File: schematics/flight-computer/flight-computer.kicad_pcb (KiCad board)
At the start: 4 copper layers, 80 x 80 mm, 116 parts, among them J1 BATT, J2 CHG, J3 SWD, J4 BLACKBOX, J5 USB C, J6 GPS, J7 TELEM, J8 BMI-S-201, J9 Expansion Slot, Q1 Si9933CDY, Q2 BSS138, U1 MAX14787E, U10 LTC4002-ES8, U11 MAX604, U12 MAX604, U2 STM32F405RGT6, U3 NVT2006BQ, U4 PCA9306, U5 ICM-20789, U6 MS5611-01BA, U7 Si4463, U8 MAX-M8Q, U9 BQ29200, Y1 26M, Y2 LFTCXO068373

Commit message: Rename to Lychee
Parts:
- C1, C10, C11, C12, C13, C14, C15, C16, C17, C18, C19, C2, C20, C21, C22, C23, C24, C25, C26, C27, C28, C29, C3, C30, C31, C32, C33, C34, C35, C36, C37, C38, C39, C4, C40, C41, C42, C5, C6, C7, C8, C9: footprint Strix:C_0402 -> Lychee:C_0402
- D1, D10, D11, D12, D13, D14, D2, D3, D4, D5, D6, D7, D8, D9: footprint Strix:D_0402 -> Lychee:D_0402
- D15, D16: footprint Strix:B330 -> Lychee:B330
- H1, H2, H3, H4: footprint Strix:MountingHole_Pad -> Lychee:MountingHole_Pad
- J1: footprint Strix:Molex_Nano-Fit_105313-1103 -> Lychee:Molex_Nano-Fit_105313-1103
- J2: footprint Strix:Molex_Nano-Fit_105313-1102 -> Lychee:Molex_Nano-Fit_105313-1102
- J3: footprint Strix:Header_SWD -> Lychee:Header_SWD
- J4: footprint Strix:Molex_Nano-Fit_105314-1108 -> Lychee:Molex_Nano-Fit_105314-1108
- J5: footprint Strix:USB_C -> Lychee:USB_C
- J6, J7: footprint Strix:SMA-Edge -> Lychee:SMA-Edge
- J8: footprint Strix:BMI-S-201 -> Lychee:BMI-S-201
- J9: footprint Strix:Header_RaspberryPi -> Lychee:Header_RaspberryPi
- L1, L2, L3, L4, L5, L6, L7: footprint Strix:L_0402 -> Lychee:L_0402
- L8: footprint Strix:L_Wuerth_HCI-7050 -> Lychee:L_Wuerth_HCI-7050
- Q1: footprint Strix:Si9933CDY -> Lychee:Si9933CDY
- Q2: footprint Strix:BSS138 -> Lychee:BSS138
- R1, R10, R11, R12, R13, R14, R15, R16, R17, R18, R19, R2, R20, R21, R3, R4, R5, R6, R7, R8, R9: footprint Strix:R_0402 -> Lychee:R_0402
- U1: footprint Strix:MAX14787E -> Lychee:MAX14787E
- U10: footprint Strix:LTC4002-ES8 -> Lychee:LTC4002-ES8
- U11, U12: footprint Strix:MAX604 -> Lychee:MAX604
- U2: footprint Strix:STM32F405RGT6 -> Lychee:STM32F405RGT6
- U3: footprint Strix:NVT2006BQ -> Lychee:NVT2006BQ
- U4: footprint Strix:PCA9306 -> Lychee:PCA9306
- U5: footprint Strix:ICM-20789 -> Lychee:ICM-20789
- U6: footprint Strix:MS5611-01BA -> Lychee:MS5611-01BA
- U7: footprint Strix:Si4463 -> Lychee:Si4463
- U8: footprint Strix:MAX-M8Q -> Lychee:MAX-M8Q
- U9: footprint Strix:BQ29200 -> Lychee:BQ29200
- Y1: footprint Strix:Xtal-20x16 -> Lychee:Xtal-20x16
- Y2: footprint Strix:LFTCXO068373 -> Lychee:LFTCXO068373

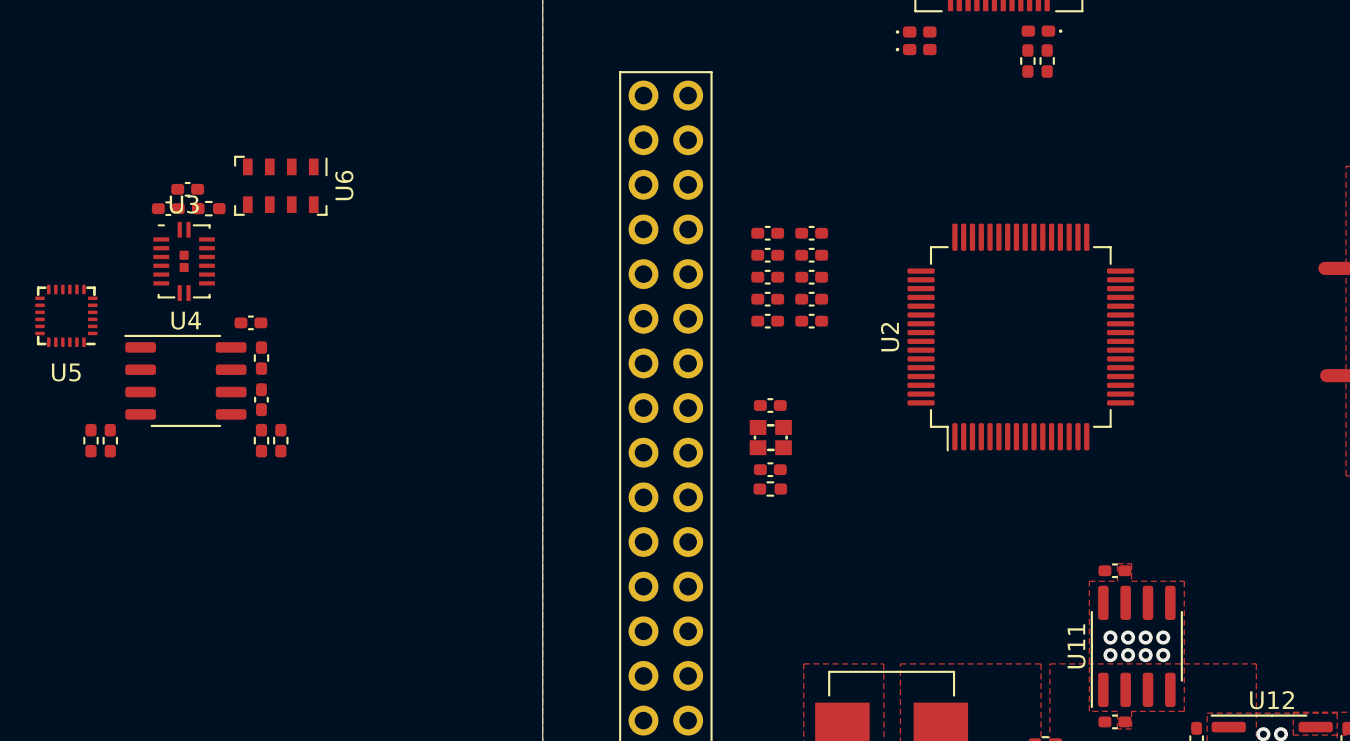
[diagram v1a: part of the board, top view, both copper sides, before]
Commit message: Fix broken model paths
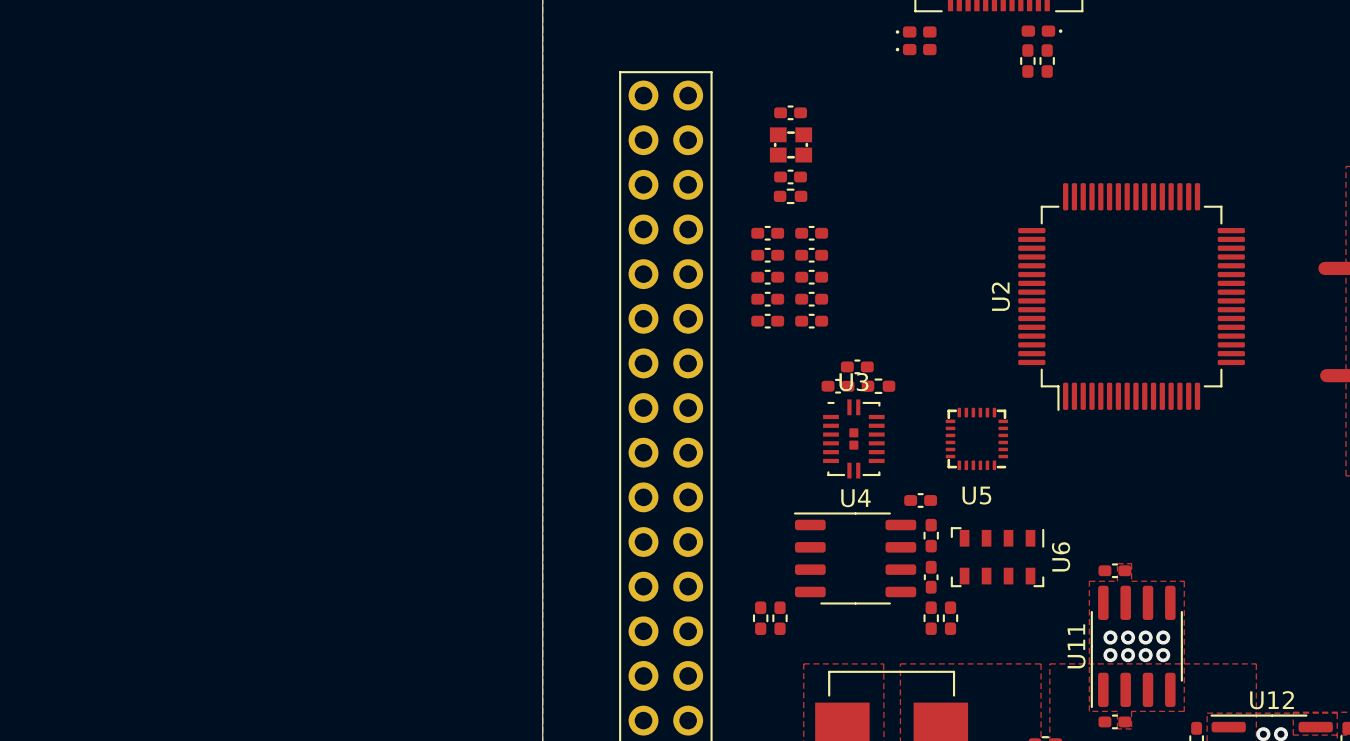
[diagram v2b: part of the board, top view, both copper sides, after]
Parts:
- U3: value NVT2006BQ -> SOT763-1 (DHVQFN16)
- moved U5 52.3 mm to (279.7, 130.4)
- moved U6 45.9 mm to (280.9, 137.1)
- moved C15 39.4 mm to (277.1, 138.3)
- moved C14 39.4 mm to (271.8, 127.4)
- moved R6 39.4 mm to (274.1, 127.4)
- moved R7 39.4 mm to (277.1, 140.6)
- moved R8 39.4 mm to (277.1, 135.9)
- moved U4 39.4 mm to (272.8, 137.2)
- moved C16 39.4 mm to (276.5, 133.9)
- moved R5 39.4 mm to (278.2, 140.6)
- moved R9 39.4 mm to (268.5, 140.6)
- moved U3 39.4 mm to (272.7, 130.4)
- moved C13 39.4 mm to (272.9, 126.3)
- moved R10 39.4 mm to (267.4, 140.6)
- moved C1 16.7 mm to (269.1, 111.8)
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
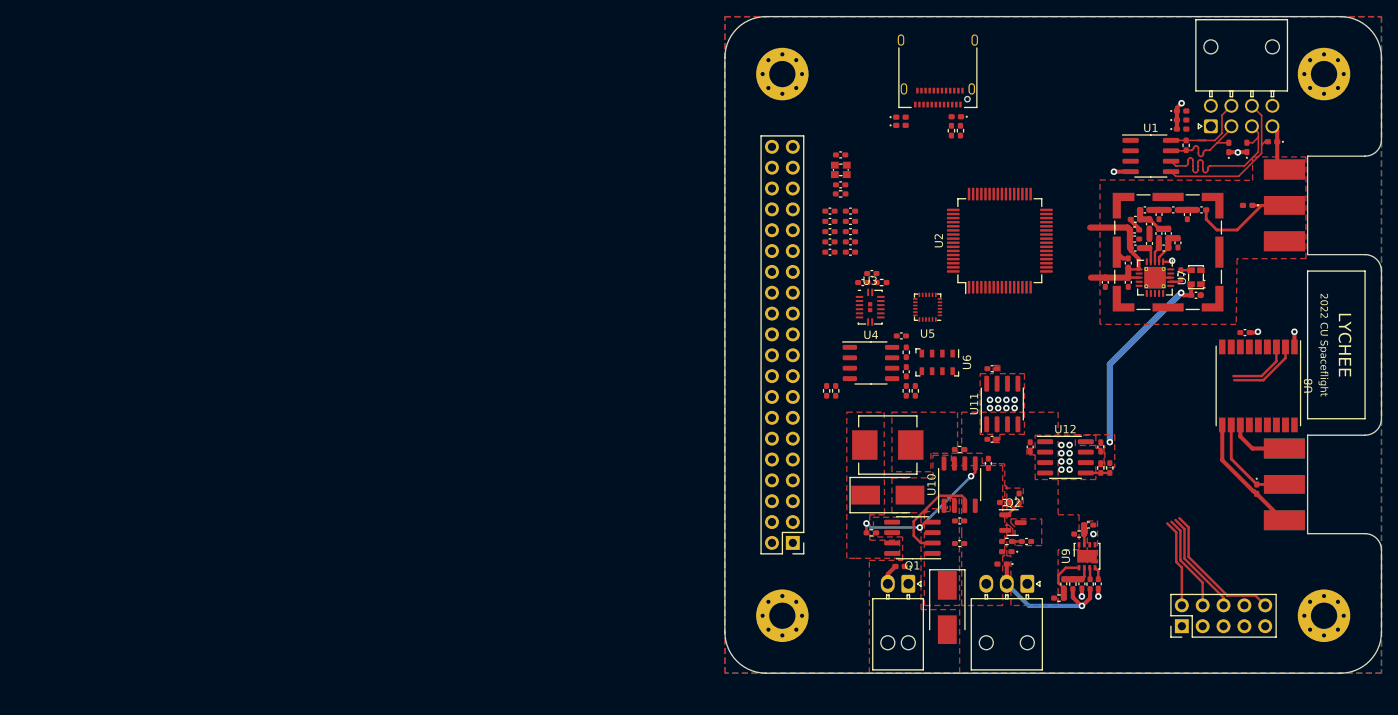
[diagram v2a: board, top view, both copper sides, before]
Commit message: Migrate to common Strix lib via submodule
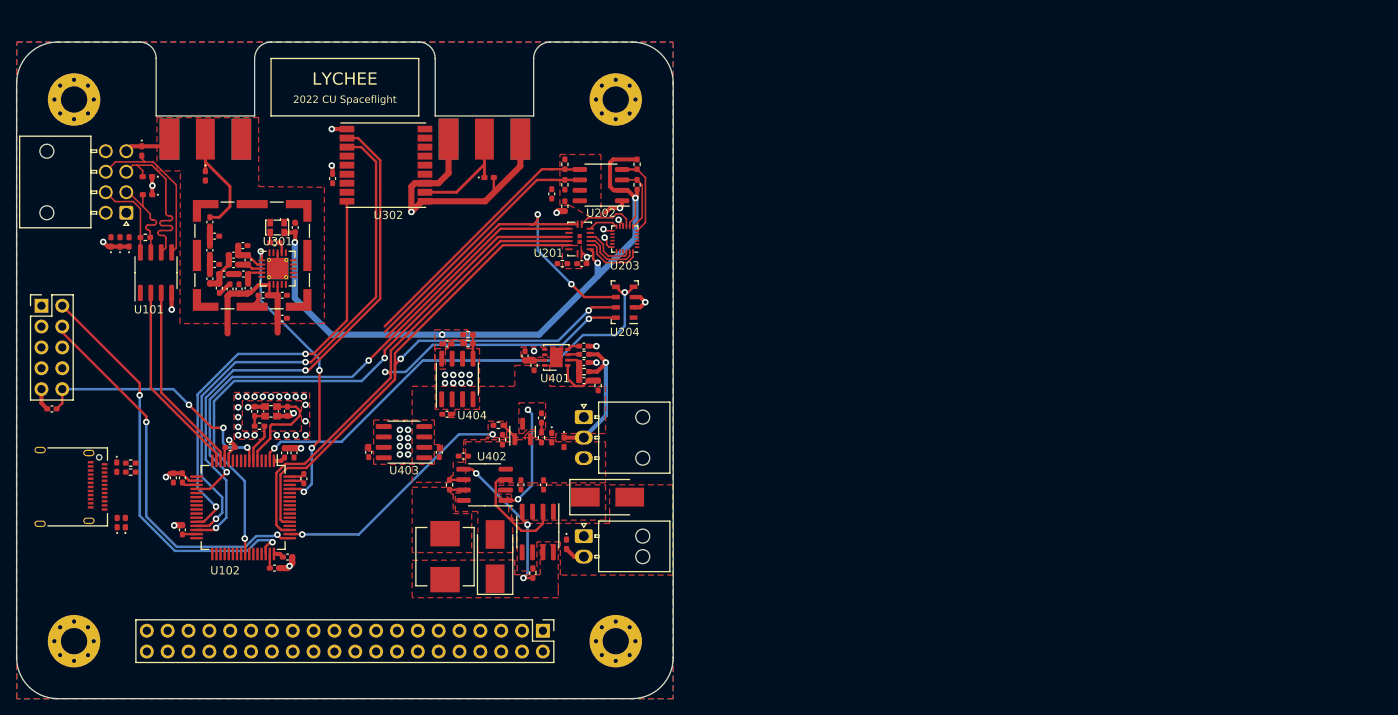
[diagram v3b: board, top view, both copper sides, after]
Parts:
- removed C14, C16: 15p, Lychee:C_0402
- removed C15: 100p, Lychee:C_0402
- removed C41, C42: 10u, Lychee:C_0402
- added C202: 100p, Strix:C_0402, F.Cu at (233.9, 116.6)
- added C411: 10u, Strix:C_0402, F.Cu at (211.6, 148.1)
- added C412: 10u, Strix:C_0402, F.Cu at (221.1, 134.9)
- C101: renamed from C4; value 4µ7 -> 1µ; footprint Lychee:C_0402 -> Strix:C_0402
- C102: renamed from C7; footprint Lychee:C_0402 -> Strix:C_0402
- C103: renamed from C1; footprint Lychee:C_0402 -> Strix:C_0402
- C104: renamed from C2; footprint Lychee:C_0402 -> Strix:C_0402
- C105: renamed from C5; footprint Lychee:C_0402 -> Strix:C_0402
- C106: renamed from C8; footprint Lychee:C_0402 -> Strix:C_0402
- C107: renamed from C6; footprint Lychee:C_0402 -> Strix:C_0402
- C108: renamed from C9; footprint Lychee:C_0402 -> Strix:C_0402
- C109: renamed from C10; footprint Lychee:C_0402 -> Strix:C_0402
- C110: renamed from C11; footprint Lychee:C_0402 -> Strix:C_0402
- C111: renamed from C12; footprint Lychee:C_0402 -> Strix:C_0402
- C112: renamed from C3; value 1µ -> 4µ7; footprint Lychee:C_0402 -> Strix:C_0402
- C201: renamed from C13; footprint Lychee:C_0402 -> Strix:C_0402
- C301: renamed from C17; footprint Lychee:C_0402 -> Strix:C_0402
- C302: renamed from C18; footprint Lychee:C_0402 -> Strix:C_0402
- C303: renamed from C19; footprint Lychee:C_0402 -> Strix:C_0402
- C304: renamed from C20; footprint Lychee:C_0402 -> Strix:C_0402
- C305: renamed from C21; footprint Lychee:C_0402 -> Strix:C_0402
- C306: renamed from C22; footprint Lychee:C_0402 -> Strix:C_0402
- C307: renamed from C23; footprint Lychee:C_0402 -> Strix:C_0402
- C308: renamed from C24; footprint Lychee:C_0402 -> Strix:C_0402
- C309: renamed from C25; footprint Lychee:C_0402 -> Strix:C_0402
- C310: renamed from C26; footprint Lychee:C_0402 -> Strix:C_0402
- C311: renamed from C27; footprint Lychee:C_0402 -> Strix:C_0402
- C312: renamed from C28; footprint Lychee:C_0402 -> Strix:C_0402
- C313: renamed from C29; footprint Lychee:C_0402 -> Strix:C_0402
- C314: renamed from C30; footprint Lychee:C_0402 -> Strix:C_0402
- C401: renamed from C31; footprint Lychee:C_0402 -> Strix:C_0402
- C402: renamed from C32; footprint Lychee:C_0402 -> Strix:C_0402
- C403: renamed from C33; footprint Lychee:C_0402 -> Strix:C_0402
- C404: renamed from C34; footprint Lychee:C_0402 -> Strix:C_0402
- C405: renamed from C35; footprint Lychee:C_0402 -> Strix:C_0402
- C406: renamed from C36; footprint Lychee:C_0402 -> Strix:C_0402
- C407: renamed from C37; footprint Lychee:C_0402 -> Strix:C_0402
- C408: renamed from C38; footprint Lychee:C_0402 -> Strix:C_0402
- C409: renamed from C39; footprint Lychee:C_0402 -> Strix:C_0402
- C410: renamed from C40; footprint Lychee:C_0402 -> Strix:C_0402
- D101: renamed from D1; footprint Lychee:D_0402 -> Strix:D_0402
- D102: renamed from D2; footprint Lychee:D_0402 -> Strix:D_0402
- D103: renamed from D3; footprint Lychee:D_0402 -> Strix:D_0402
- D104: renamed from D4; footprint Lychee:D_0402 -> Strix:D_0402
- D105: renamed from D5; footprint Lychee:D_0402 -> Strix:D_0402
- D106: renamed from D6; footprint Lychee:D_0402 -> Strix:D_0402
- D107: renamed from D7; footprint Lychee:D_0402 -> Strix:D_0402
- D108: renamed from D8; footprint Lychee:D_0402 -> Strix:D_0402
- D109: renamed from D9; footprint Lychee:D_0402 -> Strix:D_0402
- D110: renamed from D10; footprint Lychee:D_0402 -> Strix:D_0402
- D111: renamed from D11; footprint Lychee:D_0402 -> Strix:D_0402
- D112: renamed from D12; footprint Lychee:D_0402 -> Strix:D_0402
- D113: renamed from D13; footprint Lychee:D_0402 -> Strix:D_0402
- D114: renamed from D14; footprint Lychee:D_0402 -> Strix:D_0402
- D401: renamed from D15; footprint Lychee:B330 -> Strix:B330
- D402: renamed from D16; footprint Lychee:B330 -> Strix:B330
- H101: renamed from H1; footprint Lychee:MountingHole_Pad -> Strix:MountingHole_Pad
- H102: renamed from H2; footprint Lychee:MountingHole_Pad -> Strix:MountingHole_Pad
- H103: renamed from H3; footprint Lychee:MountingHole_Pad -> Strix:MountingHole_Pad
- H104: renamed from H4; footprint Lychee:MountingHole_Pad -> Strix:MountingHole_Pad
- J101: renamed from J1; footprint Lychee:Molex_Nano-Fit_105313-1103 -> Strix:Molex_Nano-Fit_105313-1103
- J102: renamed from J2; footprint Lychee:Molex_Nano-Fit_105313-1102 -> Strix:Molex_Nano-Fit_105313-1102
- J103: renamed from J3; value SWD -> Expansion Slot; footprint Lychee:Header_SWD -> Strix:Header_RaspberryPi
- J104: renamed from J4; value BLACKBOX -> SWD; footprint Lychee:Molex_Nano-Fit_105314-1108 -> Strix:Header_SWD
- J105: renamed from J5; value USB C -> BLACKBOX; footprint Lychee:USB_C -> Strix:Molex_Nano-Fit_105314-1108
- J106: renamed from J6; value GPS -> USB C; footprint Lychee:SMA-Edge -> Strix:USB_C
- J107: renamed from J7; value TELEM -> GPS; footprint Lychee:SMA-Edge -> Strix:SMA-Edge
- J108: renamed from J8; value BMI-S-201 -> TELEM; footprint Lychee:BMI-S-201 -> Strix:SMA-Edge
- J301: renamed from J9; value Expansion Slot -> BMI-S-201; footprint Lychee:Header_RaspberryPi -> Strix:BMI-S-201
- L301: renamed from L1; footprint Lychee:L_0402 -> Strix:L_0402
- L302: renamed from L2; footprint Lychee:L_0402 -> Strix:L_0402
- L303: renamed from L3; footprint Lychee:L_0402 -> Strix:L_0402
- L304: renamed from L4; footprint Lychee:L_0402 -> Strix:L_0402
- L305: renamed from L5; footprint Lychee:L_0402 -> Strix:L_0402
- L306: renamed from L6; footprint Lychee:L_0402 -> Strix:L_0402
- L307: renamed from L7; footprint Lychee:L_0402 -> Strix:L_0402
- L401: renamed from L8; footprint Lychee:L_Wuerth_HCI-7050 -> Strix:L_Wuerth_HCI-7050
- Q401: renamed from Q1; footprint Lychee:Si9933CDY -> Strix:Si9933CDY
- Q402: renamed from Q2; footprint Lychee:BSS138 -> Strix:BSS138
- R101: renamed from R1; footprint Lychee:R_0402 -> Strix:R_0402
- R102: renamed from R2; footprint Lychee:R_0402 -> Strix:R_0402
- R103: renamed from R3; footprint Lychee:R_0402 -> Strix:R_0402
- R104: renamed from R4; footprint Lychee:R_0402 -> Strix:R_0402
- R201: renamed from R5; footprint Lychee:R_0402 -> Strix:R_0402
- R202: renamed from R6; value 200k -> 4k7; footprint Lychee:R_0402 -> Strix:R_0402
- R203: renamed from R7; value 4k7 -> 200k; footprint Lychee:R_0402 -> Strix:R_0402
- R204: renamed from R8; footprint Lychee:R_0402 -> Strix:R_0402
- R205: renamed from R9; footprint Lychee:R_0402 -> Strix:R_0402
- R206: renamed from R10; footprint Lychee:R_0402 -> Strix:R_0402
- R401: renamed from R11; footprint Lychee:R_0402 -> Strix:R_0402
- R402: renamed from R12; footprint Lychee:R_0402 -> Strix:R_0402
- R403: renamed from R13; footprint Lychee:R_0402 -> Strix:R_0402
- R404: renamed from R14; footprint Lychee:R_0402 -> Strix:R_0402
- R405: renamed from R15; footprint Lychee:R_0402 -> Strix:R_0402
- R406: renamed from R16; footprint Lychee:R_0402 -> Strix:R_0402
- R407: renamed from R18; footprint Lychee:R_0402 -> Strix:R_0402
- R408: renamed from R17; footprint Lychee:R_0402 -> Strix:R_0402
- R409: renamed from R19; footprint Lychee:R_0402 -> Strix:R_0402
- R410: renamed from R20; footprint Lychee:R_0402 -> Strix:R_0402
- R411: renamed from R21; footprint Lychee:R_0402 -> Strix:R_0402
- U101: renamed from U1; footprint Lychee:MAX14787E -> Strix:MAX14787E
- U102: renamed from U2; footprint Lychee:STM32F405RGT6 -> Strix:STM32F405RGT6
- U201: renamed from U3; value SOT763-1 (DHVQFN16) -> NVT2006BQ; footprint Lychee:NVT2006BQ -> Strix:NVT2006BQ
- U202: renamed from U4; footprint Lychee:PCA9306 -> Strix:PCA9306
- U203: renamed from U5; footprint Lychee:ICM-20789 -> Strix:ICM-20789
- U204: renamed from U6; footprint Lychee:MS5611-01BA -> Strix:MS5611-01BA
- U301: renamed from U7; footprint Lychee:Si4463 -> Strix:Si4463
- U302: renamed from U8; footprint Lychee:MAX-M8Q -> Strix:MAX-M8Q
- U401: renamed from U9; footprint Lychee:BQ29200 -> Strix:BQ29200
- U402: renamed from U10; footprint Lychee:LTC4002-ES8 -> Strix:LTC4002-ES8
- U403: renamed from U11; footprint Lychee:MAX604 -> Strix:MAX604
- U404: renamed from U12; footprint Lychee:MAX604 -> Strix:MAX604
- Y101: renamed from Y1; footprint Lychee:Xtal-20x16 -> Strix:Xtal-20x16
- Y301: renamed from Y2; footprint Lychee:LFTCXO068373 -> Strix:LFTCXO068373
- moved H102 152.3 mm to (175.7, 105.1), turned to 90 degrees
- moved J106 148.8 mm to (174.4, 152.3)
- moved J104 144.2 mm to (171.7, 130.2), turned to 0 degrees
- moved D109 137.8 mm to (183.9, 111.4), turned to -90 degrees
- moved D104 134.0 mm to (184.6, 114.5), turned to 180 degrees
- moved D105 131.9 mm to (184.6, 116.7), turned to 180 degrees
- moved J107 131.7 mm to (191.7, 109.9), turned to 0 degrees
- moved D106 131.4 mm to (180.2, 122.5), turned to 90 degrees
- moved D107 130.2 mm to (181.3, 122.5), turned to 90 degrees
- moved D108 129.0 mm to (182.4, 122.5), turned to 90 degrees
- moved R101 127.3 mm to (184.4, 121.9), turned to 0 degrees
- moved D114 127.1 mm to (191.7, 114.4), turned to -90 degrees
- moved U101 122.0 mm to (185.7, 126.2), turned to 90 degrees
- moved L307 120.8 mm to (192.2, 120.0), turned to 90 degrees
- moved C314 118.6 mm to (192.8, 121.8), turned to 0 degrees
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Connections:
- C201 pad 2: 3v3 -> Net-(C201-Pad2)
- D110 pad 2: Net-(D10-Pad2) -> Net-(D110-Pad2)
- J103 pad 10: /NRST -> /EXT_RX
- J103 pad 2: /SWDIO -> unconnected-(J103-Pad2)
- J103 pad 3: GND -> /EXT_SDA
- J103 pad 4: /SWCLK -> unconnected-(J103-Pad4)
- J103 pad 5: GND -> /EXT_SCL
- J103 pad 6: /SWO -> GND
- J103 pad 8: unconnected-(J3-Pad8) -> /EXT_TX
- J104 pad 2: 3v3 -> /SWDIO
- J104 pad 3: /BB_RX- -> GND
- J104 pad 4: /BB_RX+ -> /SWDCLK
- J104 pad 5: /BB_TX- -> GND
- J104 pad 6: /BB_TX+ -> unconnected-(J104-Pad6)
- J104 pad 7: GND -> unconnected-(J104-Pad7)
- J104 pad 8: GND -> unconnected-(J104-Pad8)
- J107 pad 1: /Radio/ANT_TLM -> /Radio/ANT_GPS
- J108 pad 1: GND -> /Radio/ANT_TLM
- J301 pad 1: 3v3 -> GND
- R104 pad 2: Net-(D10-Pad2) -> Net-(D110-Pad2)
- R201 pad 1: 3v3 -> Net-(C202-Pad2)
- R202 pad 1: 3v3 -> Net-(C202-Pad2)
- R202 pad 2: Net-(C14-Pad2) -> /IMU_PR_DA
- R203 pad 2: /IMU_PR_DA -> Net-(C201-Pad2)
- R204 pad 2: Net-(C16-Pad2) -> Net-(C202-Pad2)
- U201 pad 11: /IMU_~{CS} -> unconnected-(U201-Pad11)
- U201 pad 12: /SPI3_SCLK -> /IMU_~{CS}
- U201 pad 13: /SPI3_MOSI -> /SPI3_SCLK
- U201 pad 14: /SPI3_MISO -> /SPI3_MOSI
- U201 pad 15: 3v3 -> Net-(C201-Pad2)
- U201 pad 16: Net-(C14-Pad2) -> Net-(C201-Pad2)
- U201 pad 3: Net-(U3-Pad3) -> Net-(U201-Pad3)
- U201 pad 4: Net-(U3-Pad4) -> Net-(U201-Pad4)
- U201 pad 5: Net-(U3-Pad5) -> Net-(U201-Pad5)
- U201 pad 6: Net-(U3-Pad6) -> unconnected-(U201-Pad6)
- U201 pad 8: unconnected-(U3-Pad8) -> Net-(U201-Pad8)
- U201 pad 9: unconnected-(U3-Pad9) -> /SPI3_MISO
- U202 pad 7: 3v3 -> Net-(C202-Pad2)
- U202 pad 8: Net-(C16-Pad2) -> Net-(C202-Pad2)
- U203 pad 22: Net-(U3-Pad6) -> Net-(U201-Pad5)
- U203 pad 23: Net-(U3-Pad3) -> Net-(U201-Pad4)
- U203 pad 24: Net-(U3-Pad5) -> Net-(U201-Pad3)
- U203 pad 9: Net-(U3-Pad4) -> Net-(U201-Pad8)
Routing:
- net /SPI3_SCLK: track 0.00 -> 89.2 mm, vias 0 -> 2
- net /SPI3_MOSI: track 0.00 -> 86.4 mm, vias 0 -> 2
- net /IMU_~{CS}: track 0.00 -> 72.3 mm, vias 0 -> 2
- net /IMU_INT: track 0.00 -> 66.6 mm, vias 0 -> 2
- net /USART3_RX: track 8.72 -> 68.2 mm, vias 0 -> 2
- net /USART3_TX: track 7.74 -> 66.0 mm, vias 0 -> 2
- net /BARO_~{CS}: track 0.00 -> 57.4 mm, vias 0 -> 2
- net 1v8: track 24.5 -> 81.1 mm, vias 2 -> 4
- net /GPS_~{RESET}: track 0.00 -> 54.4 mm, vias 0 -> 2
- net /SWDCLK: track 0.00 -> 47.2 mm, vias 0 -> 2
- net /SPI3_MISO: track 0.00 -> 47.1 mm, vias 0 -> 2
- net GND: track 48.7 -> 94.5 mm, vias 24 -> 58
- net /SWDIO: track 10.7 -> 50.0 mm, vias 0 -> 2
- net /RADIO_SDN: track 1.15 -> 36.1 mm, vias 1 -> 4
- net Net-(C201-Pad2): track 0.00 -> 31.7 mm
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- added copper zone on F.Cu, net Net-(C202-Pad2)
- added copper zone on F.Cu, net Net-(C302-Pad2)
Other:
- outline, holes or cut-outs redrawn

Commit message: Update layout and models
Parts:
- U201: value NVT2006BQ -> SOT763-1 (DHVQFN16)

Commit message: Route oscillator
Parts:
- U201: value SOT763-1 (DHVQFN16) -> NVT2006BQ
- Y101: footprint Strix:Xtal-20x16 -> Strix:Xtal_SMD_2016
- moved R102 2.80 mm to (195.7, 143.9), turned to -90 degrees
- moved J104 2.73 mm to (174.4, 129.8)
- moved C111 2.73 mm to (175.7, 142.4)
- moved C103 2.15 mm to (199.7, 143.9), turned to -90 degrees
- moved Y101 2.15 mm to (197.7, 143.9), turned to 90 degrees
- moved C104 1.33 mm to (197.7, 141.8), turned to 180 degrees
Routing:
- net /NRST: track 31.1 -> 2.70 mm, vias 3 -> 0
- net /SWDIO: track 50.0 -> 29.8 mm, vias 2 -> 1
- net /SWDCLK: track 47.2 -> 31.3 mm, vias 2 -> 1
- net Net-(C103-Pad2): track 12.6 -> 6.09 mm
- net GND: track 94.5 -> 96.9 mm, vias 58 -> 38
- net Net-(R102-Pad2): track 4.78 -> 5.70 mm
